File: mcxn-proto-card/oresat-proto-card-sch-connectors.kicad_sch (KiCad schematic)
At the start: 11 parts, among them J1 J-SAMTEC-TFM-110-01-L-D-RA, J2 U.FL, J3 U.FL, J4 U.FL, J6 J-SAMTEC-TFM-120-X1-XXX-D-RA

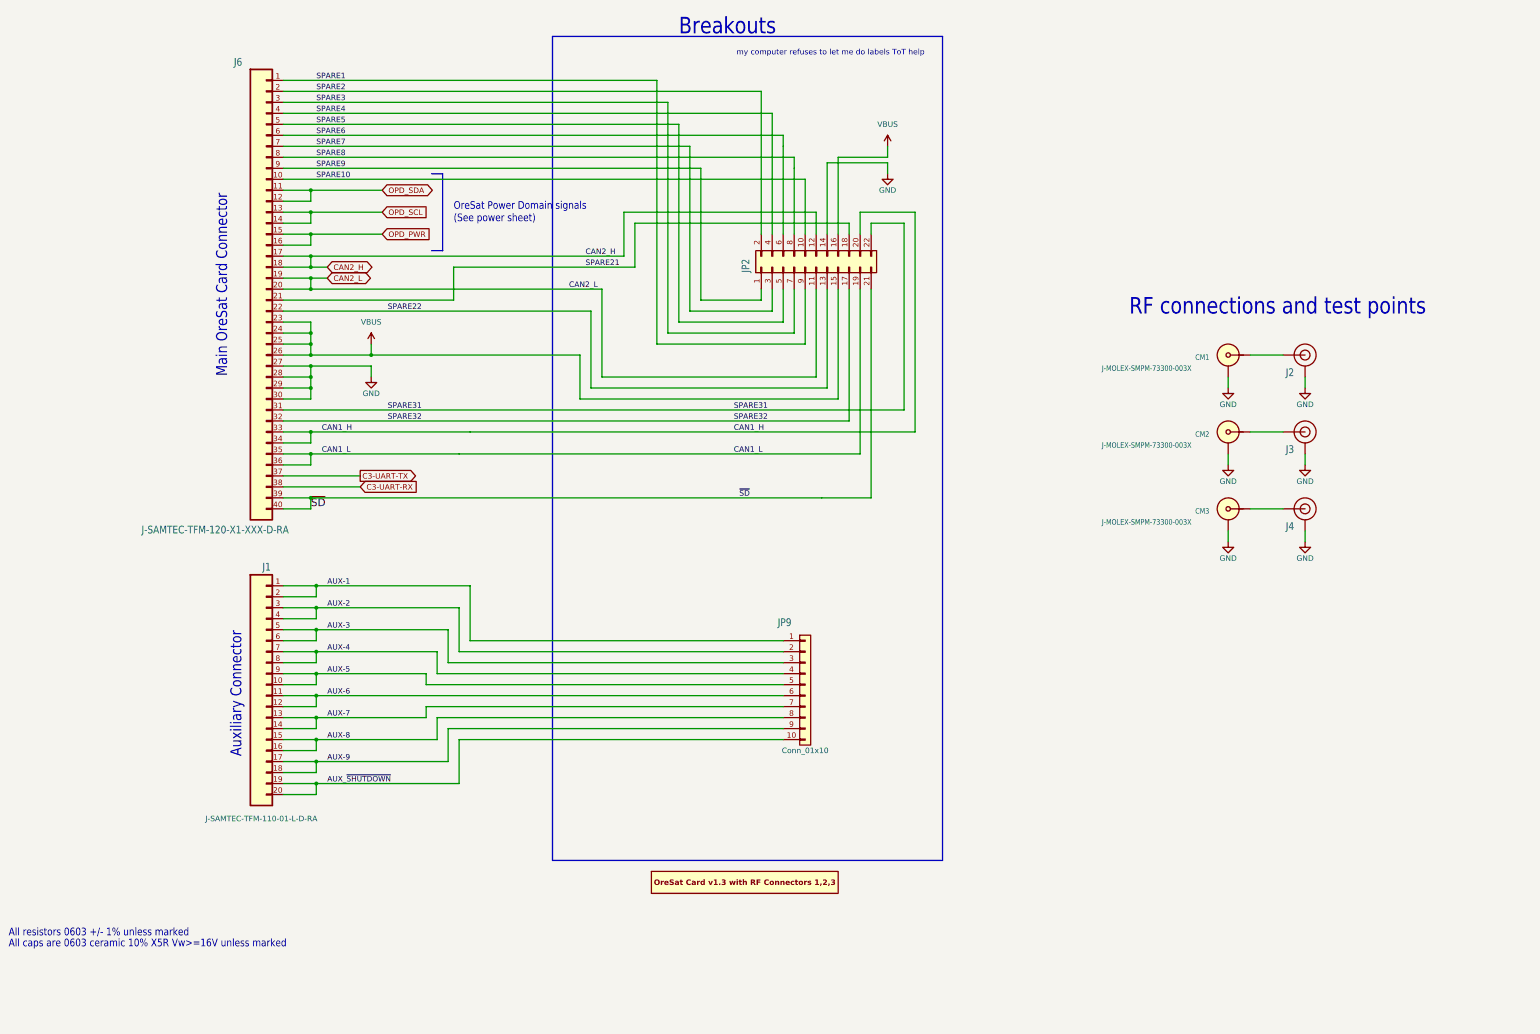
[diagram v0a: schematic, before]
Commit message: Fully routed MCXN947 proto card, still needs final polish.
Big cleanup of the proto card's OPD, bringing it up to modern standards. Also fixed the v2 backplane connector. Added the MCXN937 processor, and breakouts for the unused pins. Switched to the new debug connector, which will be fun. That's it!
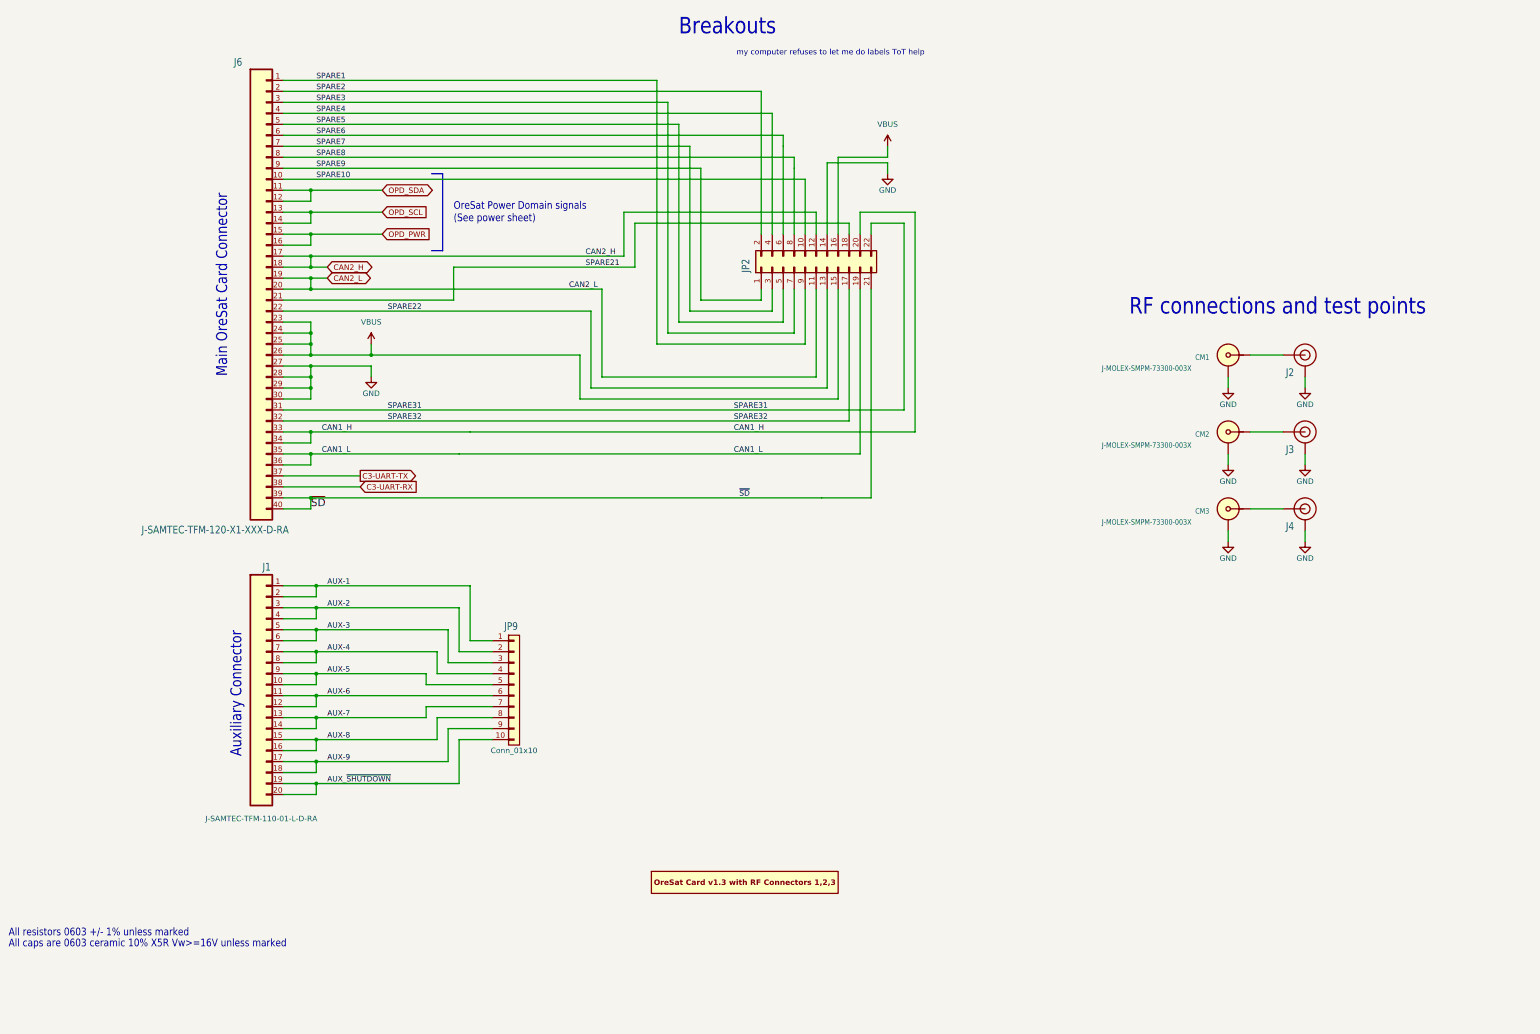
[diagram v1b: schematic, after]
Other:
- title: OreSat M0 Proto Card: Connectors -> OreSat MCXN Proto Card
- moved on the sheet: JP9
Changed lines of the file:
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@@
 	(paper "USLedger")
 	(title_block
-		(title "OreSat M0 Proto Card: Connectors")
-		(date "2025-06-29")
-		(rev "5.0")
-	)
-	(rectangle
-		(start 140.97 38.1)
-		(end 231.14 228.6)
-		(stroke
-			(width 0)
-			(type default)
-		)
-		(fill
-			(type none)
-		)
+		(title "OreSat MCXN Proto Card")
+		(date "2025-11-13")
+		(rev "6.0")
 	)
 	(text "Auxiliary Connector"
@@
 	(wire
 		(pts
-			(xy 119.38 200.66) (xy 194.31 200.66)
+			(xy 119.38 200.66) (xy 127 200.66)
 		)
 		(stroke
@@
 	(wire
 		(pts
-			(xy 111.76 187.96) (xy 194.31 187.96)
+			(xy 111.76 187.96) (xy 127 187.96)
 		)
 		(stroke
@@
 	(wire
 		(pts
-			(xy 114.3 195.58) (xy 194.31 195.58)
+			(xy 114.3 195.58) (xy 127 195.58)
 		)
 		(stroke
@@
 	(wire
 		(pts
-			(xy 116.84 182.88) (xy 194.31 182.88)
+			(xy 116.84 182.88) (xy 127 182.88)
 		)
 		(stroke
@@
 	(wire
 		(pts
-			(xy 121.92 177.8) (xy 194.31 177.8)
+			(xy 121.92 177.8) (xy 127 177.8)
 		)
 		(stroke
@@
 	(wire
 		(pts
-			(xy 114.3 185.42) (xy 194.31 185.42)
+			(xy 114.3 185.42) (xy 127 185.42)
 		)
 		(stroke
@@
 	(wire
 		(pts
-			(xy 111.76 193.04) (xy 194.31 193.04)
+			(xy 111.76 193.04) (xy 127 193.04)
 		)
 		(stroke
@@
 	(wire
 		(pts
-			(xy 119.38 180.34) (xy 194.31 180.34)
+			(xy 119.38 180.34) (xy 127 180.34)
 		)
 		(stroke
@@
 	(wire
 		(pts
-			(xy 86.36 190.5) (xy 194.31 190.5)
+			(xy 86.36 190.5) (xy 127 190.5)
 		)
 		(stroke
@@
 	(wire
 		(pts
-			(xy 116.84 198.12) (xy 194.31 198.12)
+			(xy 116.84 198.12) (xy 127 198.12)
 		)
 		(stroke
@@
 	(symbol
 		(lib_id "Connector_Generic:Conn_01x10")
-		(at 199.39 187.96 0)
+		(at 132.08 187.96 0)
 		(unit 1)
 		(exclude_from_sim no)
@@
 		(dnp no)
 		(property "Reference" "JP9"
-			(at 193.04 174.625 0)
+			(at 129.794 175.514 0)
 			(effects
 				(font
@@
 		)
 		(property "Value" "Conn_01x10"
-			(at 199.39 203.2 0)
+			(at 132.08 203.2 0)
 			(effects
 				(font
@@
 		)
 		(property "Footprint" "Connector_PinHeader_2.54mm:PinHeader_1x10_P2.54mm_Vertical"
-			(at 199.39 187.96 0)
+			(at 132.08 187.96 0)
 			(effects
 				(font
@@
 		)
 		(property "Datasheet" "~"
-			(at 199.39 187.96 0)
+			(at 132.08 187.96 0)
 			(effects
 				(font
@@
 		)
 		(property "Description" "Generic connector, single row, 01x10, script generated (kicad-library-utils/schlib/autogen/connector/)"
-			(at 199.39 187.96 0)
+			(at 132.08 187.96 0)
 			(effects
 				(font
@@
 		)
 		(property "DIS" "Digi-Key"
-			(at 199.39 187.96 0)
+			(at 132.08 187.96 0)
 			(effects
 				(font
@@
 		)
 		(property "DPN" "732-5329-ND "
-			(at 199.39 187.96 0)
+			(at 132.08 187.96 0)
 			(effects
 				(font
@@
 		)
 		(property "MFR" "Wurth"
-			(at 199.39 187.96 0)
+			(at 132.08 187.96 0)
 			(effects
 				(font
@@
 		)
 		(property "MPN" "61302011121"
-			(at 199.39 187.96 0)
+			(at 132.08 187.96 0)
 			(effects
 				(font

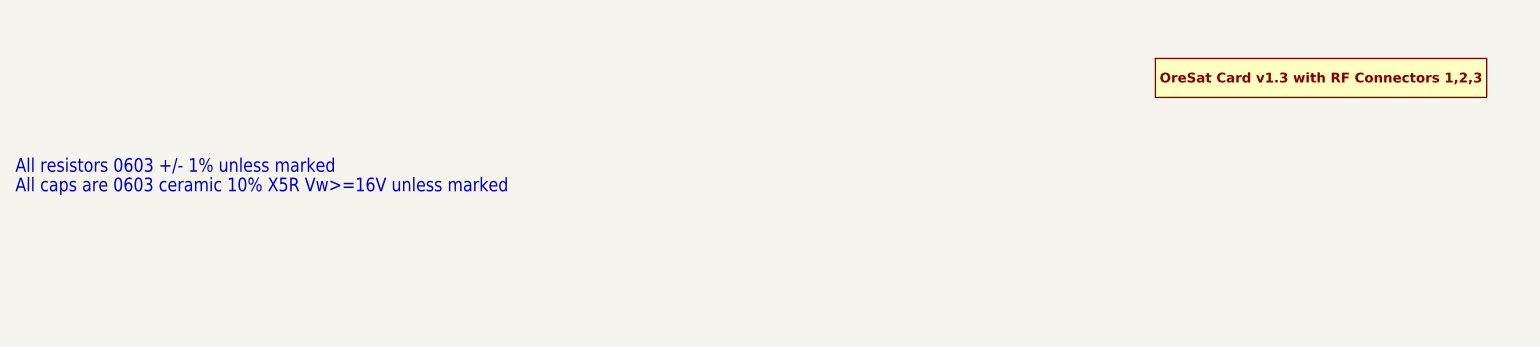
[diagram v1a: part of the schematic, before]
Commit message: Final MCXN protocard cleanup
Made schematic fancy with hierarchical pins, cleaned up schematics a bit, and fixed silk screen a ton. Ready for fab.
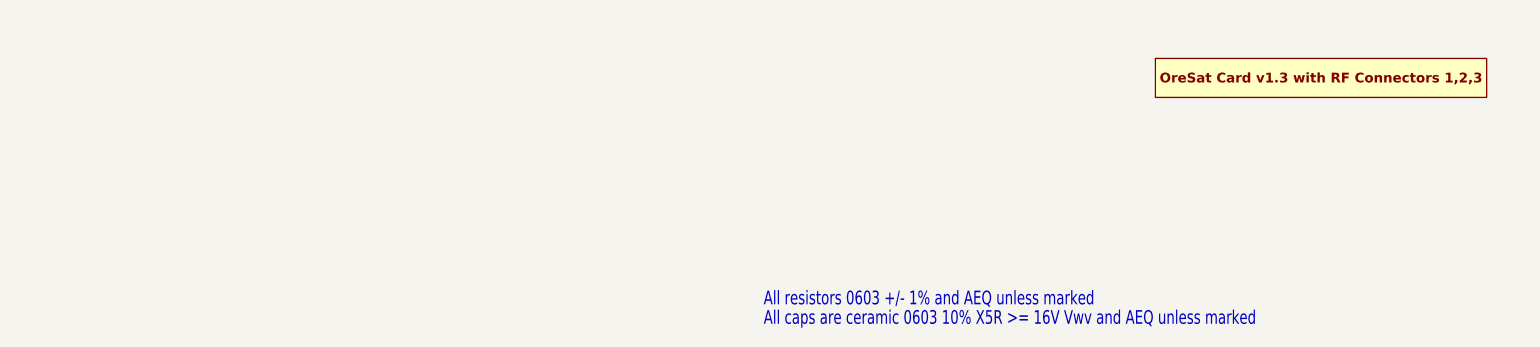
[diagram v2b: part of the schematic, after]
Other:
- note added: "All caps are ceramic 0603 10% X5R >= 16V Vwv and AEQ unless marked"
- note added: "All resistors 0603 +/- 1% and AEQ unless marked"
- note removed: "All caps are 0603 ceramic 10% X5R Vw>=16V unless marked"
- note removed: "All resistors 0603 +/- 1% unless marked"
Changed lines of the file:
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@@
 		)
 	)
-	(text "All resistors 0603 +/- 1% unless marked"
+	(text "All resistors 0603 +/- 1% and AEQ unless marked"
 		(exclude_from_sim no)
-		(at 15.24 246.38 0)
+		(at 112.776 263.652 0)
 		(effects
 			(font
-				(size 1.778 1.5113)
+				(size 1.778 1.27)
 			)
 			(justify left bottom)
@@
 		)
 	)
+	(text "All caps are ceramic 0603 10% X5R >= 16V Vwv and AEQ unless marked"
+		(exclude_from_sim no)
+		(at 112.776 266.192 0)
+		(effects
+			(font
+				(size 1.778 1.27)
+			)
+			(justify left bottom)
+		)
+	)
 	(text "OreSat Power Domain signals\n(See power sheet)"
 		(exclude_from_sim no)
@@
 		(effects
 			(font
-				(size 1.778 1.5113)
-			)
-			(justify left bottom)
-		)
-	)
-	(text "All caps are 0603 ceramic 10% X5R Vw>=16V unless marked"
-		(exclude_from_sim no)
-		(at 15.24 248.92 0)
-		(effects
-			(font
